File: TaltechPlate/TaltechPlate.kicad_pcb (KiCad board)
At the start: 2 copper layers, 150 x 150 mm, 8 parts, among them J1 Conn_01x02, J2 Conn_01x04

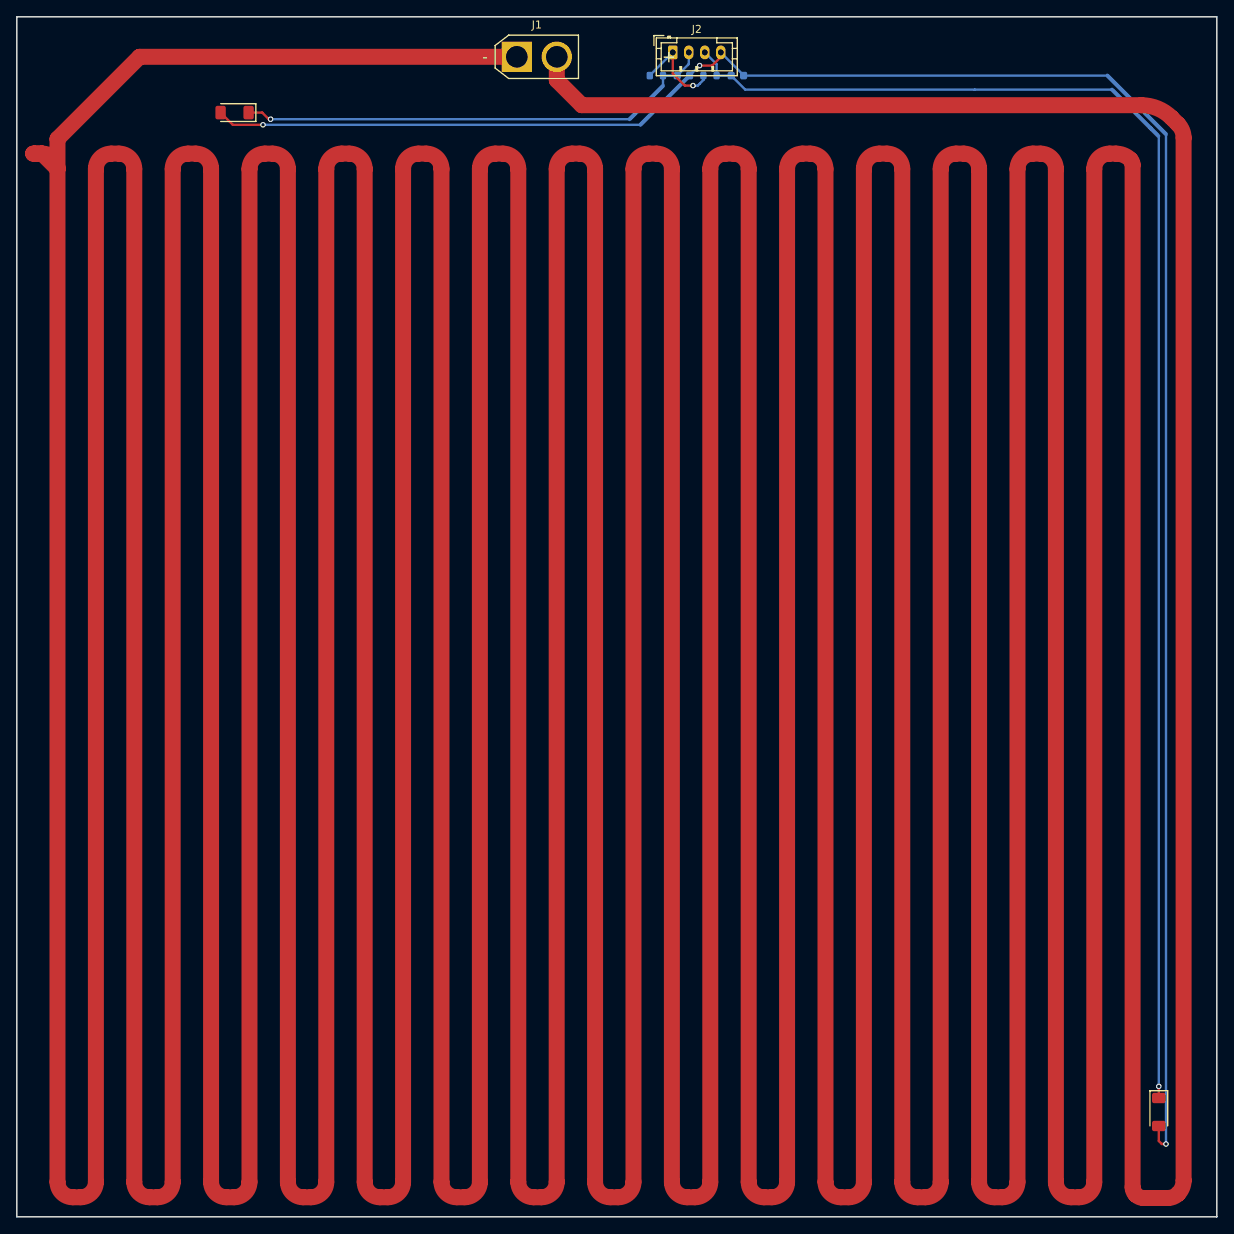
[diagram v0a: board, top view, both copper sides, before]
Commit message: Mounting holes and longer trace on plate
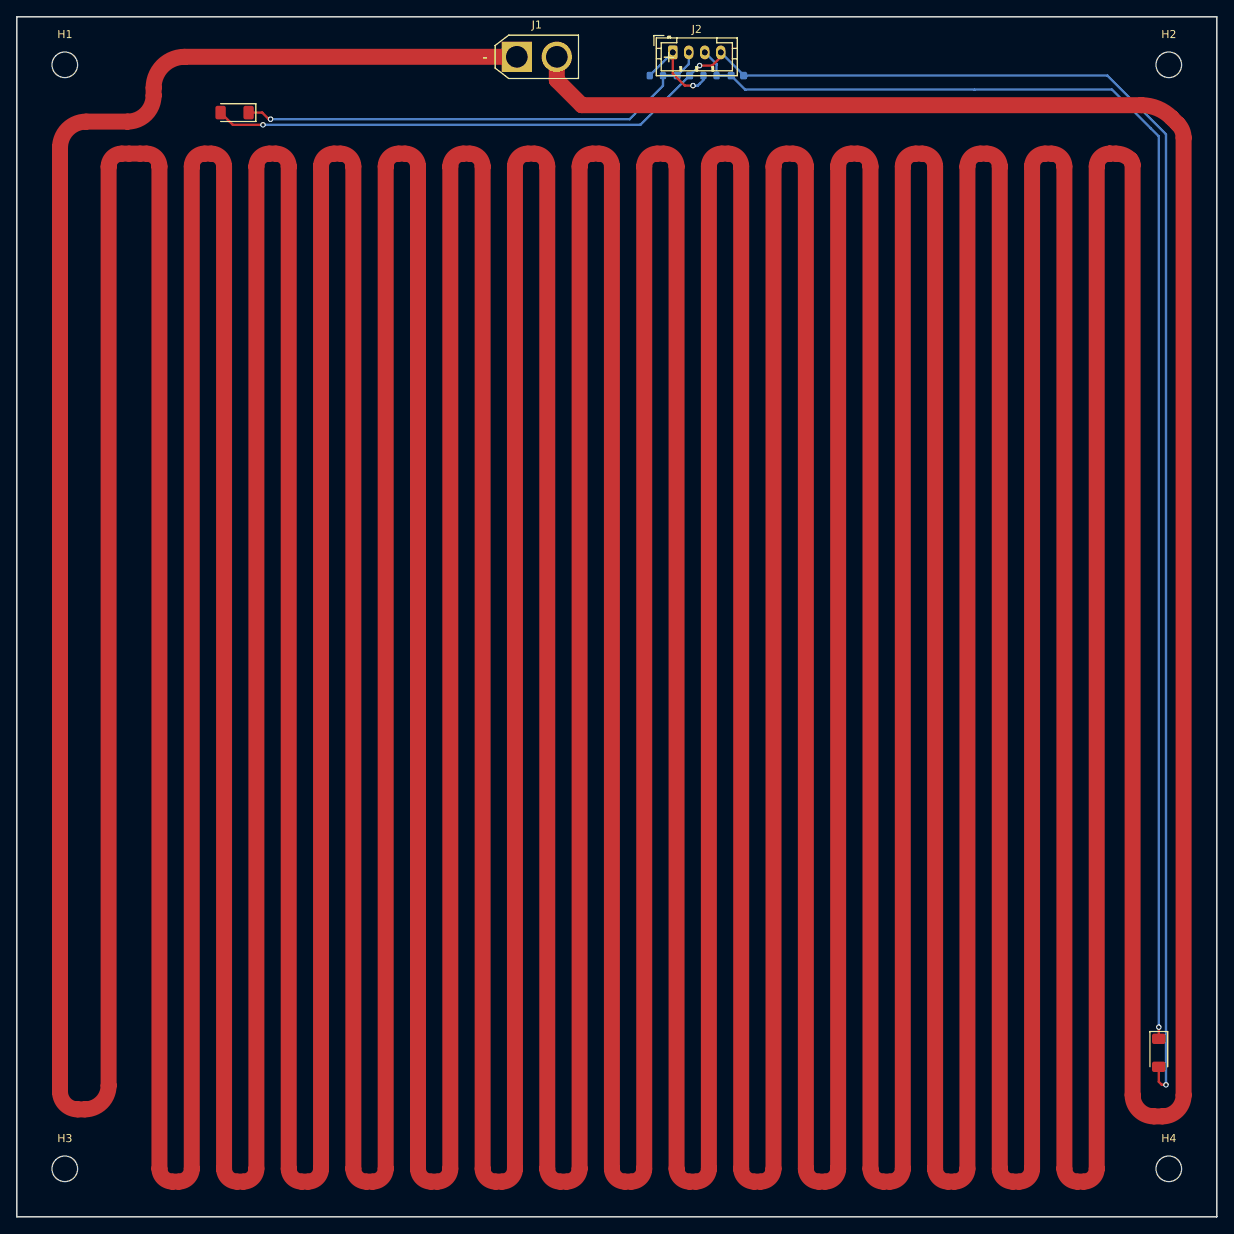
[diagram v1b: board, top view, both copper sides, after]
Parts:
- added G***: LOGO, AA:Taltech, B.Cu at (156.9, 79.6)
- added H1: Mounting hole, MountingHole:MountingHole_3.2mm_M3_DIN965, F.Cu at (30.1, 40.0)
- added H2: Mounting hole, MountingHole:MountingHole_3.2mm_M3_DIN965, F.Cu at (168.1, 40.0)
- added H3: Mounting hole, MountingHole:MountingHole_3.2mm_M3_DIN965, F.Cu at (30.1, 178.0)
- added H4: Mounting hole, MountingHole:MountingHole_3.2mm_M3_DIN965, F.Cu at (168.1, 178.0)
- moved TH2 7.40 mm to (166.9, 163.5)
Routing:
- net Net-(J1-Pin_1): track 4160.8 -> 4573.9 mm
- net GND: track 256.3 -> 248.9 mm
- net /NTC_2: track 182.1 -> 174.7 mm
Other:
- board text added: "Heat Plate"
- board text added: "Rev 1.1"
- board text added: "Robin Madar Taavi Salum"
